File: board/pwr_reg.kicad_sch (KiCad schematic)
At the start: 52 parts, among them J2 9V-30VDC, Q1 IRF9540N, Q2 2N3906, Q3 IRF9540N, Q4 2N3906, SW1 On/Off, SW2 RESET, U1 LM350, U2 LM350, U3 LM350

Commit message: Re-structure schematics and improve safety.
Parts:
- C1, C? (x2): footprint (none) -> Capacitor_THT:C_Disc_D5.0mm_W2.5mm_P5.00mm
- C10, C11, C12, C4, C5, C6, C7, C8, C9: footprint (none) -> Capacitor_THT:C_Radial_D6.3mm_H5.0mm_P2.50mm
- D10, D11, D9: footprint (none) -> LED_THT:LED_D3.0mm
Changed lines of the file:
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@@
       (effects (font (size 1.27 1.27)) (justify left))
     )
-    (property "Footprint" "" (id 2) (at 113.9952 66.04 0)
+    (property "Footprint" "Capacitor_THT:C_Disc_D5.0mm_W2.5mm_P5.00mm" (id 2) (at 113.9952 66.04 0)
       (effects (font (size 1.27 1.27)) hide)
     )
@@
       (effects (font (size 1.27 1.27)) (justify left))
     )
-    (property "Footprint" "" (id 2) (at 140.6652 68.58 0)
+    (property "Footprint" "Capacitor_THT:C_Radial_D6.3mm_H5.0mm_P2.50mm" (id 2) (at 140.6652 68.58 0)
       (effects (font (size 1.27 1.27)) hide)
     )
@@
       (effects (font (size 1.27 1.27)) (justify left))
     )
-    (property "Footprint" "" (id 2) (at 41.6052 146.05 0)
+    (property "Footprint" "Capacitor_THT:C_Disc_D5.0mm_W2.5mm_P5.00mm" (id 2) (at 41.6052 146.05 0)
       (effects (font (size 1.27 1.27)) hide)
     )
@@
       (effects (font (size 1.27 1.27)) (justify left))
     )
-    (property "Footprint" "" (id 2) (at 82.2452 139.7 0)
+    (property "Footprint" "Capacitor_THT:C_Radial_D6.3mm_H5.0mm_P2.50mm" (id 2) (at 82.2452 139.7 0)
       (effects (font (size 1.27 1.27)) hide)
     )
@@
       (effects (font (size 1.27 1.27)) (justify left))
     )
-    (property "Footprint" "" (id 2) (at 200.3552 144.78 0)
+    (property "Footprint" "Capacitor_THT:C_Radial_D6.3mm_H5.0mm_P2.50mm" (id 2) (at 200.3552 144.78 0)
       (effects (font (size 1.27 1.27)) hide)
     )
@@
       (effects (font (size 1.27 1.27)) (justify left))
     )
-    (property "Footprint" "" (id 2) (at 171.1452 62.23 0)
+    (property "Footprint" "Capacitor_THT:C_Radial_D6.3mm_H5.0mm_P2.50mm" (id 2) (at 171.1452 62.23 0)
       (effects (font (size 1.27 1.27)) hide)
     )
@@
       (effects (font (size 1.27 1.27)) (justify right))
     )
-    (property "Footprint" "" (id 2) (at 187.96 62.23 0)
+    (property "Footprint" "LED_THT:LED_D3.0mm" (id 2) (at 187.96 62.23 0)
       (effects (font (size 1.27 1.27)) hide)
     )
@@
       (effects (font (size 1.27 1.27)) (justify left))
     )
-    (property "Footprint" "" (id 2) (at 227.0252 139.7 0)
+    (property "Footprint" "Capacitor_THT:C_Radial_D6.3mm_H5.0mm_P2.50mm" (id 2) (at 227.0252 139.7 0)
       (effects (font (size 1.27 1.27)) hide)
     )
@@
       (effects (font (size 1.27 1.27)) (justify left))
     )
-    (property "Footprint" "" (id 2) (at 68.2752 146.05 0)
+    (property "Footprint" "Capacitor_THT:C_Radial_D6.3mm_H5.0mm_P2.50mm" (id 2) (at 68.2752 146.05 0)
       (effects (font (size 1.27 1.27)) hide)
     )
@@
       (effects (font (size 1.27 1.27)) (justify left))
     )
-    (property "Footprint" "" (id 2) (at 172.4152 140.97 0)
+    (property "Footprint" "Capacitor_THT:C_Disc_D5.0mm_W2.5mm_P5.00mm" (id 2) (at 172.4152 140.97 0)
       (effects (font (size 1.27 1.27)) hide)
     )
@@
       (effects (font (size 1.27 1.27)) (justify left))
     )
-    (property "Footprint" "" (id 2) (at 96.2152 139.7 0)
+    (property "Footprint" "Capacitor_THT:C_Radial_D6.3mm_H5.0mm_P2.50mm" (id 2) (at 96.2152 139.7 0)
       (effects (font (size 1.27 1.27)) hide)
     )
@@
       (effects (font (size 1.27 1.27)) (justify left))
     )
-    (property "Footprint" "" (id 2) (at 213.0552 139.7 0)
+    (property "Footprint" "Capacitor_THT:C_Radial_D6.3mm_H5.0mm_P2.50mm" (id 2) (at 213.0552 139.7 0)
       (effects (font (size 1.27 1.27)) hide)
     )
@@
       (effects (font (size 1.27 1.27)) (justify left))
     )
-    (property "Footprint" "" (id 2) (at 150.8252 62.23 0)
+    (property "Footprint" "Capacitor_THT:C_Radial_D6.3mm_H5.0mm_P2.50mm" (id 2) (at 150.8252 62.23 0)
       (effects (font (size 1.27 1.27)) hide)
     )
@@
       (effects (font (size 1.27 1.27)) (justify right))
     )
-    (property "Footprint" "" (id 2) (at 240.03 138.43 0)
+    (property "Footprint" "LED_THT:LED_D3.0mm" (id 2) (at 240.03 138.43 0)
       (effects (font (size 1.27 1.27)) hide)
     )
@@
       (effects (font (size 1.27 1.27)) (justify right))
     )
-    (property "Footprint" "" (id 2) (at 109.22 142.24 0)
-      (effects (font (size 1.27 1.27)) hide)
-    )
+    (property "Footprint" "LED_THT:LED_D3.0mm" (id 2) (at 109.22 142.24 0)
+      (effects (font (size 1.27 1.27)) hide)
+    )

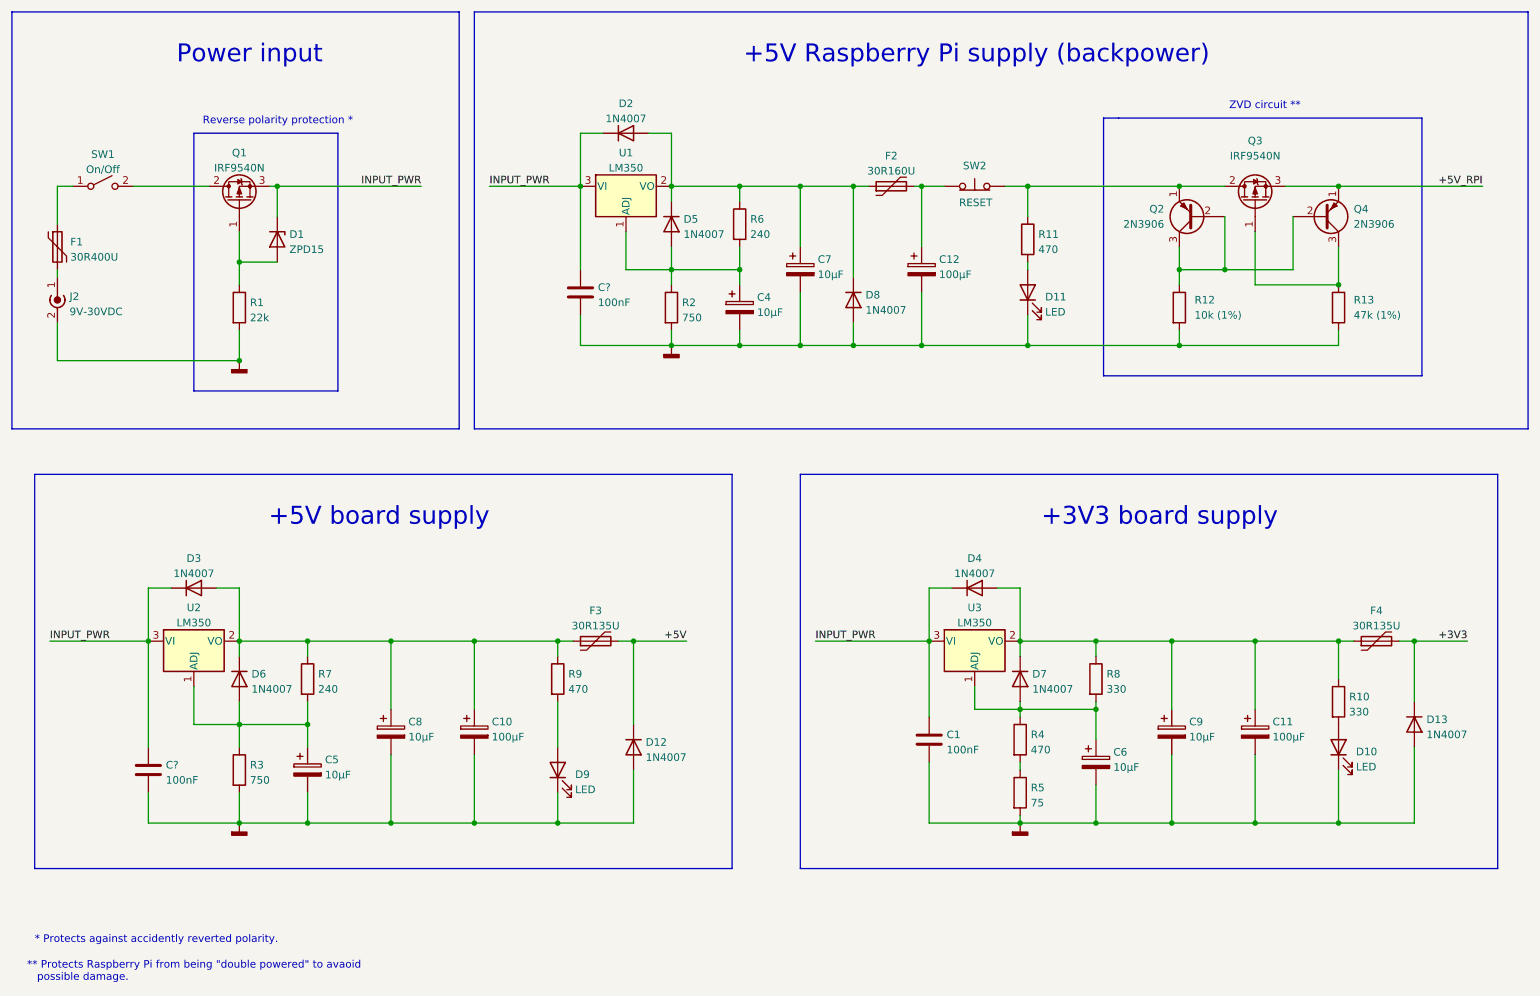
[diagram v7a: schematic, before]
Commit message: Add missing footprints.
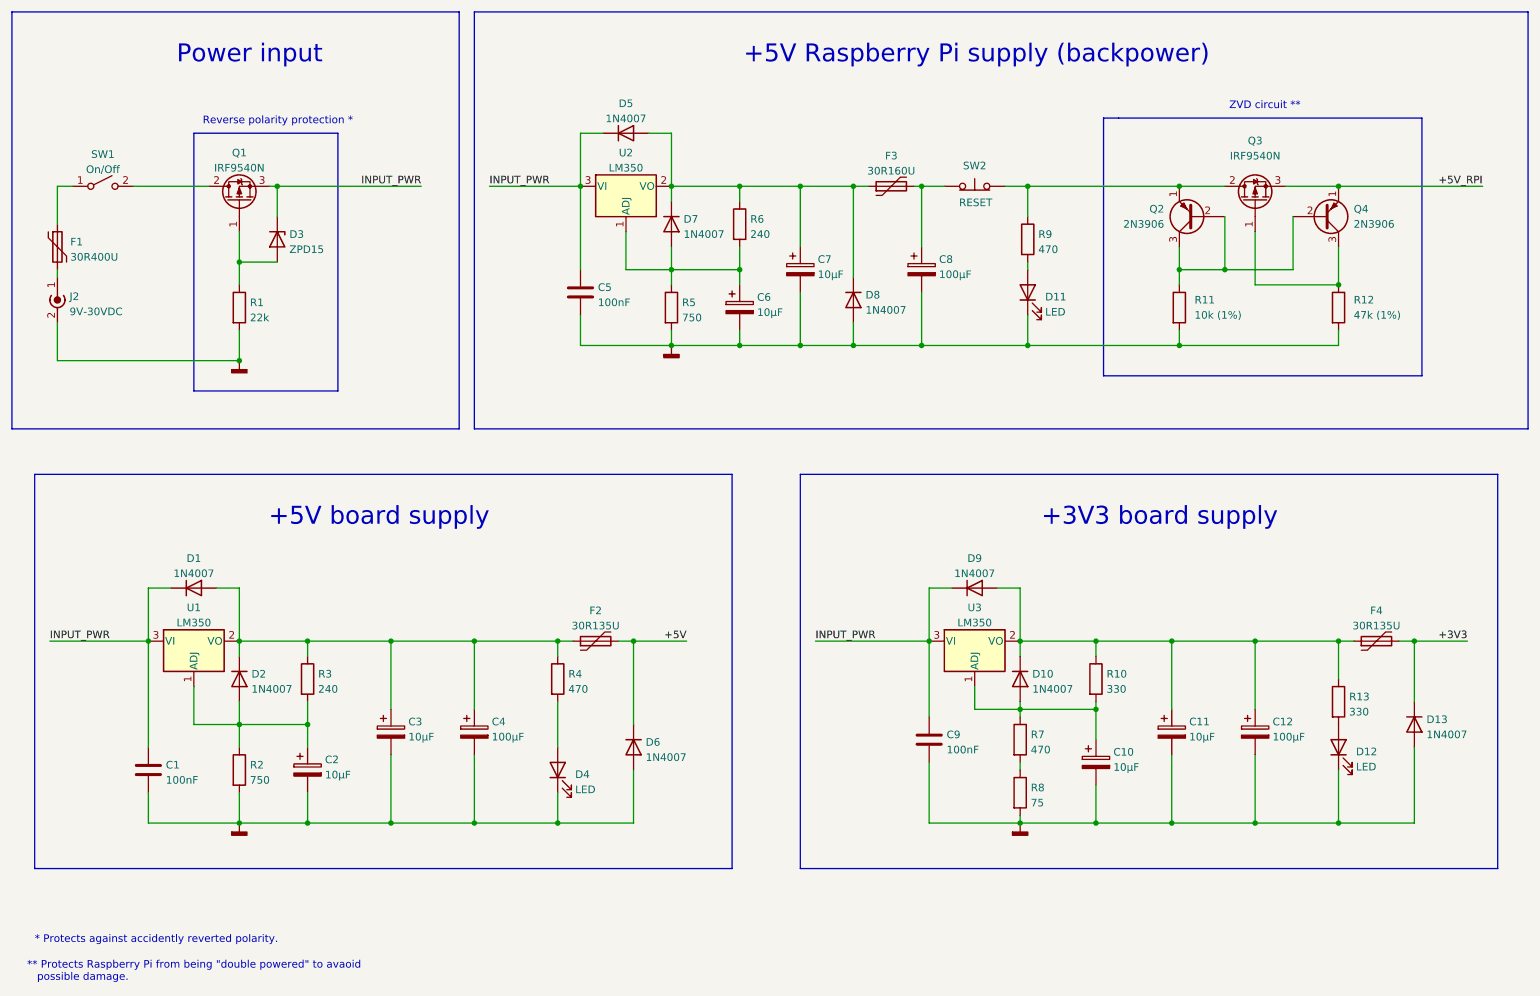
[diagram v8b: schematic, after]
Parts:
- J2: footprint Connector_Wire:SolderWire-2sqmm_1x02_P7.8mm_D2mm_OD3.9mm -> Connector_Wire:SolderWire-1.5sqmm_1x02_P6mm_D1.7mm_OD3mm
- SW1: footprint Connector_Wire:SolderWire-0.5sqmm_1x02_P4.8mm_D0.9mm_OD2.3mm -> Connector_Wire:SolderWire-1.5sqmm_1x02_P7.8mm_D1.7mm_OD3.9mm
- SW2: footprint (none) -> Connector_Wire:SolderWire-0.5sqmm_1x02_P4.8mm_D0.9mm_OD2.3mm
- gave numbers to parts that had none: 2
- renumbered C6 to C10, C9 to C11, C11 to C12, C5 to C2, C8 to C3, C10 to C4, C4 to C6, C12 to C8, C1 to C9, D3 to D1, D7 to D10, D10 to D12, D6 to D2, D1 to D3, D9 to D4, D2 to D5, D12 to D6, D5 to D7, D4 to D9, F3 to F2, F2 to F3, R8 to R10, R12 to R11, R13 to R12, R10 to R13, R3 to R2, R7 to R3, R9 to R4, R2 to R5, R4 to R7, R5 to R8, R11 to R9, U2 to U1, U1 to U2
